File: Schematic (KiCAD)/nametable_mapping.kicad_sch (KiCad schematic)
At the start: 42 parts

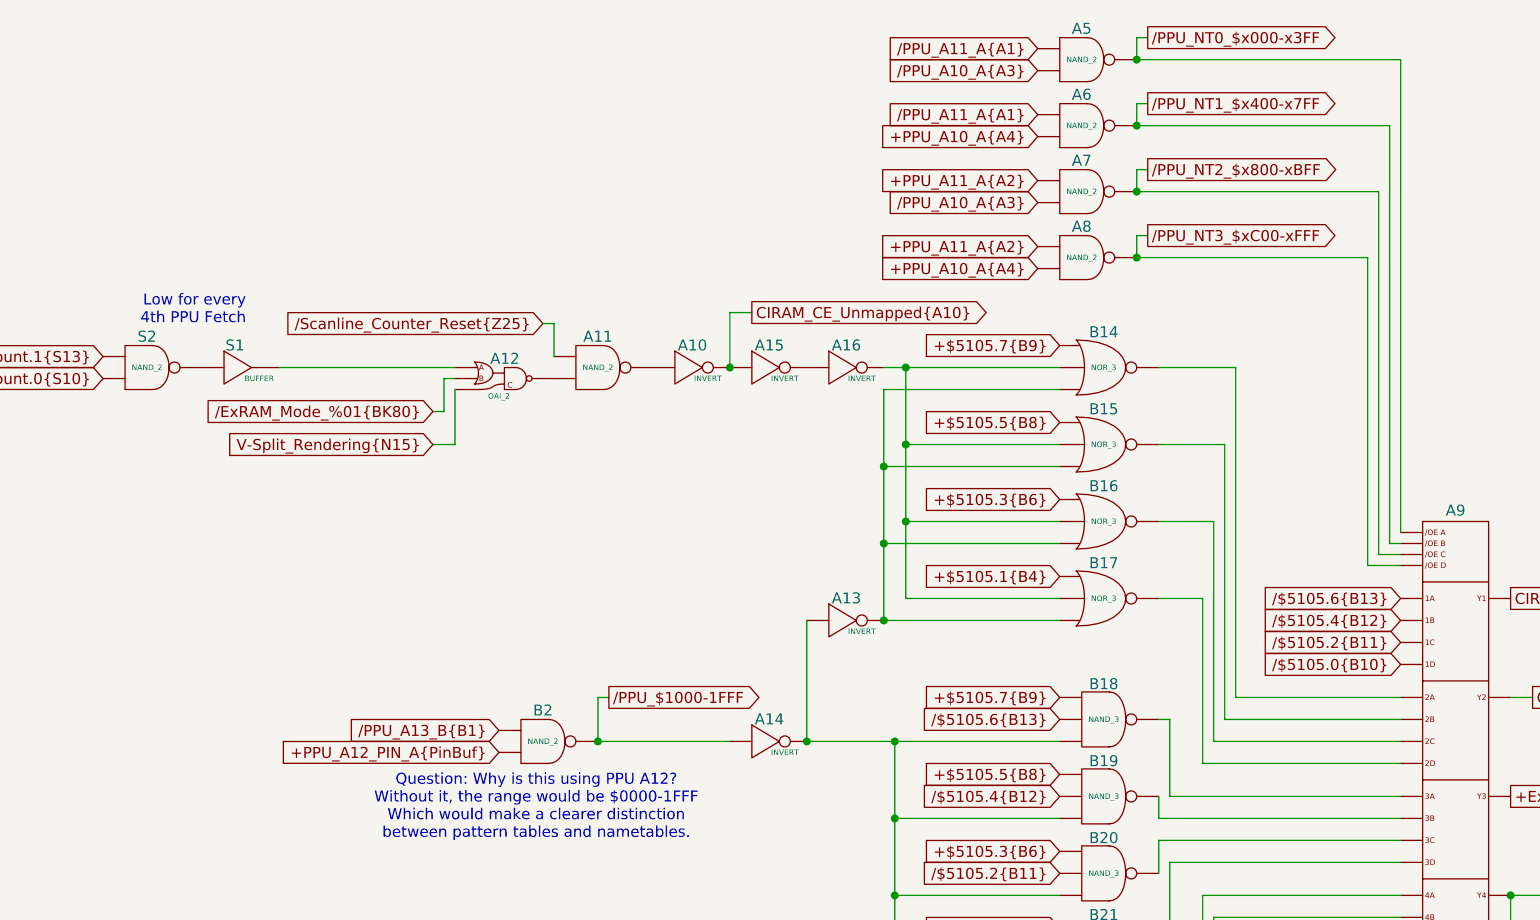
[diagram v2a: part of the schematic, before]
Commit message: Tracing and schematic updates.  - Added timer to schematic.  - Added all items from artifacts sheet to the MMC5A trace.
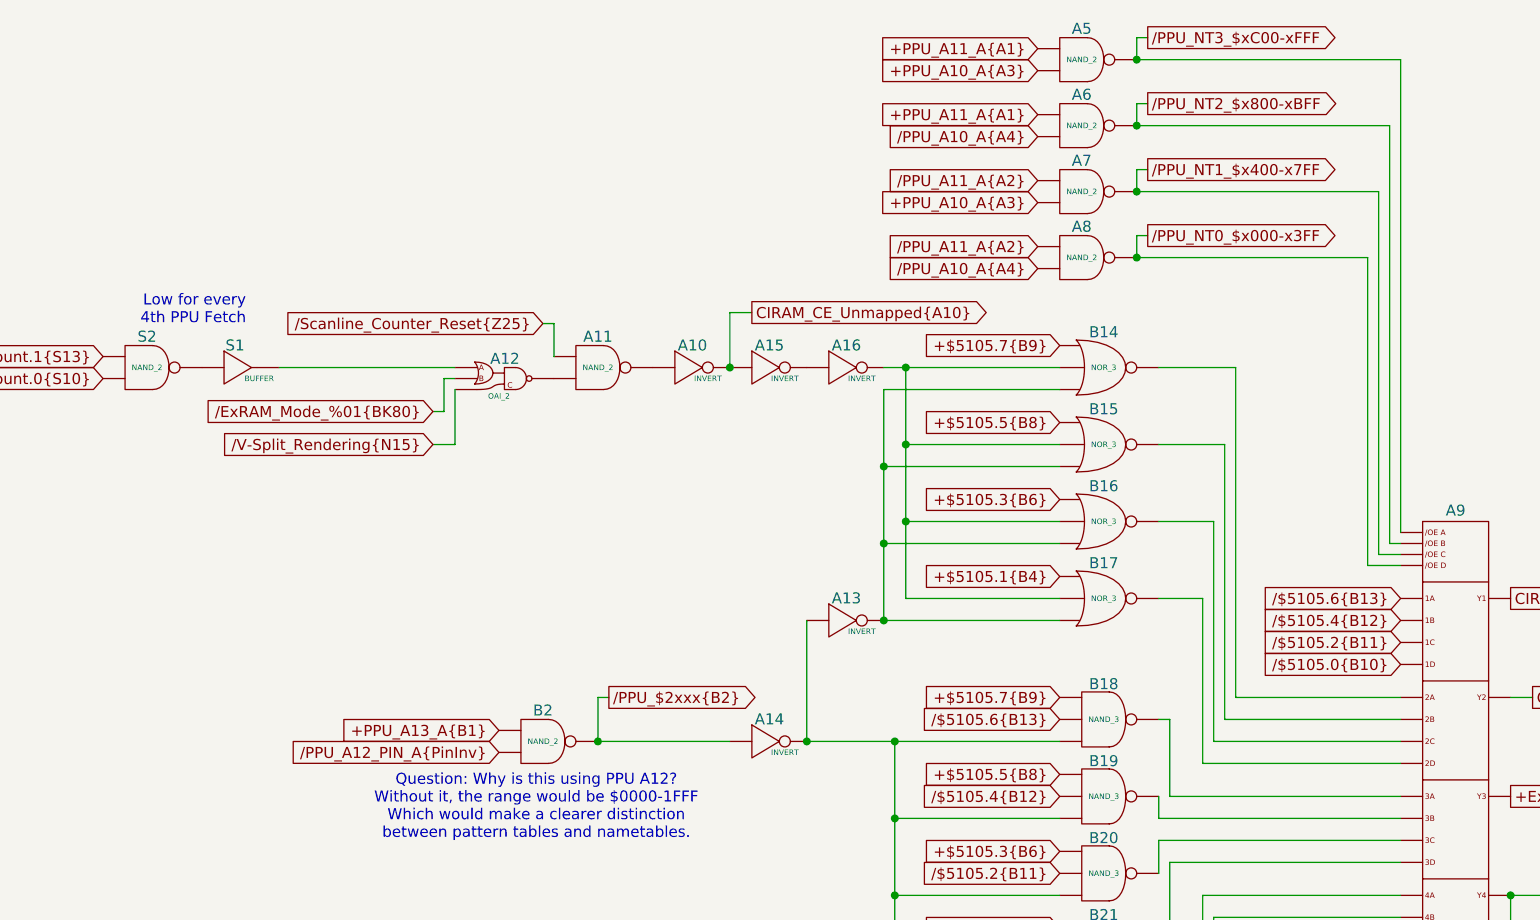
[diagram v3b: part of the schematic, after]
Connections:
- net V-Split_Rendering{N15} is gone; now on net /V-Split_Rendering{N15}: A12. (X)
- net /PPU_A13_B{B1} is gone; now on net /PPU_A12_PIN_A{PinInv}: B2. (X)
- net /PPU_NT0_$x000-x3FF: now also A8. (X); no longer A5. (X)
- net /PPU_NT1_$x400-x7FF: now also A7. (X); no longer A6. (X)
- net /PPU_NT2_$x800-xBFF: now also A6. (X); no longer A7. (X)
- net /PPU_NT3_$xC00-xFFF: now also A5. (X); no longer A8. (X)
- net at S1. (X): now also A12. (X); no longer S2. (X)
- net /V-Split_Rendering{N15}: now reaches A12. (X)
- net /V-Split_Rendering{N15}: no longer A11. (X)
- removed net +PPU_A10_A{A4}: A6. (X), A8. (X)
- removed net +PPU_A11_A{A2}: A7. (X), A8. (X)
- net +PPU_A12_PIN_A{PinBuf} renamed /PPU_A12_PIN_A{PinInv}
- net /PPU_$1000-1FFF renamed /PPU_$2xxx{B2}
- removed net /PPU_A10_A{A3}: A5. (X), A7. (X)
- removed net /PPU_A11_A{A1}: A5. (X), A6. (X)
- new net: B9. (X), C1. (/Q7)
- new net: A13. (X), A14. (X), B18. (X), B19. (X), B20. (X), B21. (X), B22. (X), B23. (X), B24. (X), B25. (X)
- new net: A9. (Y4), B25. (X)
- new net: B6. (X), C1. (/Q7)
- new net: A9. (Y4), B23. (X)
- new net: A16. (X), B14. (X), B15. (X), B16. (X), B17. (X)
- new net: A13. (X), B14. (X), B15. (X), B16. (X), B17. (X)
- new net: A9. (Y4), B16. (X)
- new net: S1. (X), S2. (X)
- new net: B10. (X), C1. (/Q7)
- new net: A9. (Y4), B15. (X)
- new net: B7. (X), C1. (/Q7)
- new net: A11. (X), A12. (X)
- new net: A10. (X), A11. (X)
- new net: B4. (X), C1. (/Q7)
- new net: BL11. (X), BL33. (X)
- new net: B11. (X), C1. (/Q7)
- new net: B3. (X), C1. (/Q7)
- new net: A9. (Y4), B22. (X)
- new net: A17. (X), C1. (/Q7)
- new net: A9. (Y4), B14. (X)
- new net: A9. (Y4), B21. (X)
- new net: A9. (Y4), B18. (X)
- new net: A9. (Y4), B20. (X)
- new net: A9. (Y4), B19. (X)
- new net: A9. (Y4), B17. (X)
- new net: A9. (Y4), B24. (X)
- new net: B13. (X), C1. (/Q7)
- new net: B12. (X), C1. (/Q7)
- new net: B5. (X), C1. (/Q7)
- new net: B8. (X), C1. (/Q7)
- new net +PPU_A10_A{A3}: A5. (X), A7. (X)
- new net +PPU_A11_A{A1}: A5. (X), A6. (X)
- new net +PPU_A13_A{B1}: B2. (X)
- new net /PPU_A10_A{A4}: A6. (X), A8. (X)
- new net /PPU_A11_A{A2}: A7. (X), A8. (X)
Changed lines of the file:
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@@
-	(wire
-		(pts
-			(xy 194.31 34.29) (xy 193.04 34.29)
-		)
-		(stroke
-			(width 0)
-			(type default)
-		)
-	)
 	(wire
 		(pts
@@
 	(wire
 		(pts
+			(xy 193.04 49.53) (xy 194.31 49.53)
+		)
+		(stroke
+			(width 0)
+			(type default)
+		)
+	)
+	(wire
+		(pts
 			(xy 223.52 83.82) (xy 223.52 29.21)
 		)
@@
 	(wire
 		(pts
+			(xy 193.04 41.91) (xy 194.31 41.91)
+		)
+		(stroke
+			(width 0)
+			(type default)
+		)
+	)
+	(wire
+		(pts
 			(xy 146.05 64.77) (xy 146.05 58.42)
 		)
@@
 	(wire
 		(pts
-			(xy 194.31 49.53) (xy 193.04 49.53)
-		)
-		(stroke
-			(width 0)
-			(type default)
-		)
-	)
-	(wire
-		(pts
 			(xy 184.15 148.59) (xy 165.1 148.59)
 		)
@@
 	(wire
 		(pts
-			(xy 194.31 26.67) (xy 193.04 26.67)
-		)
-		(stroke
-			(width 0)
-			(type default)
-		)
-	)
-	(wire
-		(pts
-			(xy 194.31 41.91) (xy 193.04 41.91)
-		)
-		(stroke
-			(width 0)
-			(type default)
-		)
-	)
-	(wire
-		(pts
 			(xy 124.46 59.69) (xy 125.73 59.69)
 		)
@@
 	(wire
 		(pts
+			(xy 193.04 26.67) (xy 194.31 26.67)
+		)
+		(stroke
+			(width 0)
+			(type default)
+		)
+	)
+	(wire
+		(pts
 			(xy 193.04 41.91) (xy 193.04 44.45)
 		)
@@
 		(pts
 			(xy 196.85 121.92) (xy 196.85 132.08)
+		)
+		(stroke
+			(width 0)
+			(type default)
+		)
+	)
+	(wire
+		(pts
+			(xy 193.04 34.29) (xy 194.31 34.29)
 		)
 		(stroke
@@
 		)
 	)
-	(global_label "+PPU_A12_PIN_A{PinBuf}"
+	(global_label "{slash}PPU_A12_PIN_A{PinInv}"
 		(shape input)
 		(at 119.38 109.22 180)
@@
 		)
 		(property "Intersheetrefs" "${INTERSHEET_REFS}"
-			(at 92.3857 109.22 0)
-			(effects
-				(font
-					(size 1.27 1.27)
-				)
-				(justify right)
-				(hide yes)
-			)
-		)
-	)
-	(global_label "+PPU_A10_A{A4}"
+			(at 93.0509 109.22 0)
+			(effects
+				(font
+					(size 1.27 1.27)
+				)
+				(justify right)
+				(hide yes)
+			)
+		)
+	)
+	(global_label "{slash}PPU_A10_A{A4}"
 		(shape input)
 		(at 181.61 53.34 180)
@@
 		)
 		(property "Intersheetrefs" "${INTERSHEET_REFS}"
-			(at 162.659 53.34 0)
+			(at 162.9009 53.34 0)
 			(effects
 				(font
@@
 	(global_label "{slash}PPU_NT1_$x400-x7FF"
 		(shape output)
-		(at 194.31 34.29 0)
+		(at 194.31 41.91 0)
 		(fields_autoplaced yes)
 		(effects
@@
 		)
 		(property "Intersheetrefs" "${INTERSHEET_REFS}"
-			(at 219.7923 34.29 0)
+			(at 219.7923 41.91 0)
 			(effects
 				(font
@@
 		)
 	)
-	(global_label "+PPU_A10_A{A4}"
+	(global_label "{slash}PPU_A10_A{A4}"
 		(shape input)
 		(at 181.61 38.1 180)
@@
 		)
 		(property "Intersheetrefs" "${INTERSHEET_REFS}"
-			(at 162.659 38.1 0)
+			(at 162.9009 38.1 0)
 			(effects
 				(font
@@
 		)
 	)
-	(global_label "{slash}PPU_A10_A{A3}"
+	(global_label "+PPU_A10_A{A3}"
 		(shape input)
 		(at 181.61 30.48 180)
@@
 		)
 		(property "Intersheetrefs" "${INTERSHEET_REFS}"
-			(at 162.9009 30.48 0)
+			(at 162.659 30.48 0)
 			(effects
 				(font
@@
 	(global_label "{slash}PPU_NT2_$x800-xBFF"
 		(shape output)
-		(at 194.31 41.91 0)
+		(at 194.31 34.29 0)
 		(fields_autoplaced yes)
 		(effects
@@
 		)
 		(property "Intersheetrefs" "${INTERSHEET_REFS}"
-			(at 219.8528 41.91 0)
+			(at 219.8528 34.29 0)
 			(effects
 				(font
@@
 		)
 	)
-	(global_label "+PPU_A11_A{A2}"
+	(global_label "{slash}PPU_A11_A{A2}"
 		(shape input)
 		(at 181.61 50.8 180)
@@
 		)
 		(property "Intersheetrefs" "${INTERSHEET_REFS}"
-			(at 162.659 50.8 0)
+			(at 162.9009 50.8 0)
 			(effects
 				(font
@@
 		)
 	)
-	(global_label "+PPU_A11_A{A2}"
+	(global_label "{slash}PPU_A11_A{A2}"
 		(shape input)
 		(at 181.61 43.18 180)
@@
 		)
 		(property "Intersheetrefs" "${INTERSHEET_REFS}"
-			(at 162.659 43.18 0)
+			(at 162.9009 43.18 0)
 			(effects
 				(font
@@
 		)
 	)
-	(global_label "{slash}PPU_A11_A{A1}"
+	(global_label "+PPU_A11_A{A1}"
 		(shape input)
 		(at 181.61 27.94 180)
@@
 		)
 		(property "Intersheetrefs" "${INTERSHEET_REFS}"
-			(at 162.9009 27.94 0)
-			(effects
-				(font
-					(size 1.27 1.27)
-				)
-				(justify right)
-				(hide yes)
-			)
-		)
-	)
-	(global_label "{slash}PPU_A10_A{A3}"
+			(at 162.659 27.94 0)
+			(effects
+				(font
+					(size 1.27 1.27)
+				)
+				(justify right)
+				(hide yes)
+			)
+		)
+	)
+	(global_label "+PPU_A10_A{A3}"
 		(shape input)
 		(at 181.61 45.72 180)
@@
 		)
 		(property "Intersheetrefs" "${INTERSHEET_REFS}"
-			(at 162.9009 45.72 0)
+			(at 162.659 45.72 0)
 			(effects
 				(font
@@
 		)
 	)
-	(global_label "{slash}PPU_$1000-1FFF"
+	(global_label "{slash}PPU_$2xxx{B2}"
 		(shape output)
 		(at 132.08 102.87 0)
@@
 		)
 		(property "Intersheetrefs" "${INTERSHEET_REFS}"
-			(at 153.329 102.87 0)
+			(at 150.91 102.87 0)
 			(effects
 				(font
@@
 	(global_label "{slash}PPU_NT3_$xC00-xFFF"
 		(shape output)
-		(at 194.31 49.53 0)
+		(at 194.31 26.67 0)
 		(fields_autoplaced yes)
 		(effects
@@
 		)
 		(property "Intersheetrefs" "${INTERSHEET_REFS}"
-			(at 219.7319 49.53 0)
+			(at 219.7319 26.67 0)
 			(effects
 				(font
@@
 		)
 	)
-	(global_label "{slash}PPU_A13_B{B1}"
+	(global_label "+PPU_A13_A{B1}"
 		(shape input)
 		(at 119.38 106.68 180)
@@
 		)
 		(property "Intersheetrefs" "${INTERSHEET_REFS}"
-			(at 100.3081 106.68 0)
+			(at 100.2476 106.68 0)
 			(effects
 				(font
@@
 		)
 	)
-	(global_label "V-Split_Rendering{N15}"
+	(global_label "{slash}V-Split_Rendering{N15}"
 		(shape input)
 		(at 111.76 73.66 180)
@@
 		)
 		(property "Intersheetrefs" "${INTERSHEET_REFS}"
-			(at 85.9149 73.66 0)
-			(effects
-				(font
-					(size 1.27 1.27)
-				)
-				(justify right)
-				(hide yes)
-			)
-		)
-	)
-	(global_label "{slash}PPU_A11_A{A1}"
+			(at 84.5844 73.66 0)
+			(effects
+				(font
+					(size 1.27 1.27)
+				)
+				(justify right)
+				(hide yes)
+			)
+		)
+	)
+	(global_label "+PPU_A11_A{A1}"
 		(shape input)
 		(at 181.61 35.56 180)
@@
 		)
 		(property "Intersheetrefs" "${INTERSHEET_REFS}"
-			(at 162.9009 35.56 0)
+			(at 162.659 35.56 0)
 			(effects
 				(font
@@
 	(global_label "{slash}PPU_NT0_$x000-x3FF"
 		(shape output)
-		(at 194.31 26.67 0)
+		(at 194.31 49.53 0)
 		(fields_autoplaced yes)
 		(effects
@@
 		)
 		(property "Intersheetrefs" "${INTERSHEET_REFS}"
-			(at 219.7923 26.67 0)
-			(effects
-				(font
+			(at 219.7923 49.53 0)
+			(effects
+				(font

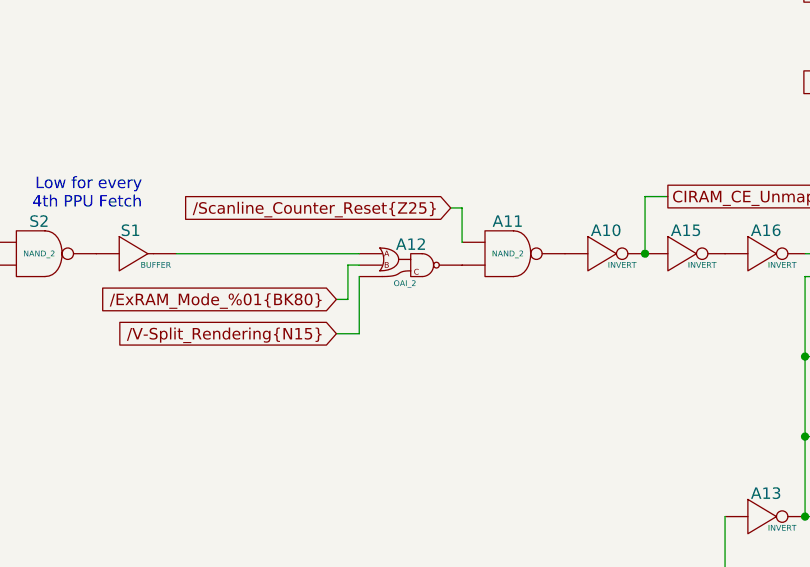
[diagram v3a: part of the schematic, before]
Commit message: - Updated all of the various And-OR-Invert gates to have consistent names.  - Added the schematic for CL3 / SL3 GPIO pins.  There are no surprises revealed by this.  - Finished up the CPU address decoding tracing.  - Added one of the 'artifact' counters from the pulse channels
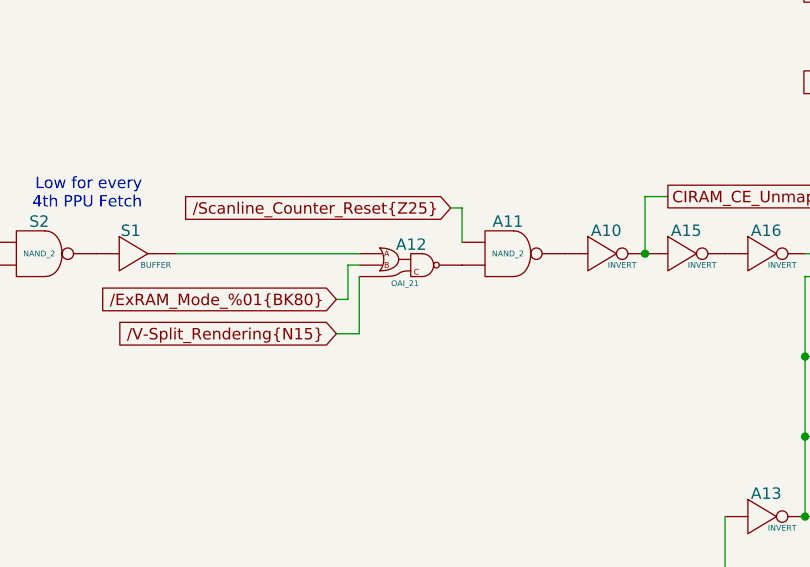
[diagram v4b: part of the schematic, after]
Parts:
- A12: value OAI_2 -> OAI_21
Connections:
- net at S1. (X): now also A12. (X); no longer S2. (X)
- new net: B9. (X), C1. (/Q7)
- new net: A13. (X), A14. (X), B18. (X), B19. (X), B20. (X), B21. (X), B22. (X), B23. (X), B24. (X), B25. (X)
- new net: A9. (Y4), B25. (X)
- new net: B6. (X), C1. (/Q7)
- new net: A9. (Y4), B23. (X)
- new net: A16. (X), B14. (X), B15. (X), B16. (X), B17. (X)
- new net: A13. (X), B14. (X), B15. (X), B16. (X), B17. (X)
- new net: A9. (Y4), B16. (X)
- new net: S1. (X), S2. (X)
- new net: B10. (X), C1. (/Q7)
- new net: A9. (Y4), B15. (X)
- new net: B7. (X), C1. (/Q7)
- new net: A11. (X), A12. (X)
- new net: A10. (X), A11. (X)
- new net: B4. (X), C1. (/Q7)
- new net: BL11. (X), BL33. (X)
- new net: B11. (X), C1. (/Q7)
- new net: B3. (X), C1. (/Q7)
- new net: A9. (Y4), B22. (X)
- new net: A17. (X), C1. (/Q7)
- new net: A9. (Y4), B14. (X)
- new net: A9. (Y4), B21. (X)
- new net: A9. (Y4), B18. (X)
- new net: A9. (Y4), B20. (X)
- new net: A9. (Y4), B19. (X)
- new net: A9. (Y4), B17. (X)
- new net: A9. (Y4), B24. (X)
- new net: B13. (X), C1. (/Q7)
- new net: B12. (X), C1. (/Q7)
- new net: B5. (X), C1. (/Q7)
- new net: B8. (X), C1. (/Q7)
